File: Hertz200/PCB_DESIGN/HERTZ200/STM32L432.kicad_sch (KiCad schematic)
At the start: 16 parts, among them J6 Conn_01x07_Male, J7 Conn_01x03_Male, SW1 SW_Push, U1 STM32L431CCUx, U6 HTS221

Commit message: layout
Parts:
- FB1: footprint (none) -> Inductor_SMD:L_0603_1608Metric
- J6: value Conn_01x07_Male -> GPIO_PINS
- J7: value Conn_01x03_Male -> SWD_PINS
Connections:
- net GND: now also J6.1 (Pin_1)
- net SIM7020E_GPIO1: now also U1.32 (PA11); no longer U1.14 (PA4)
- net VIN: now reaches J6.2 (Pin_2)
- net GPIO01: now reaches J6.3 (Pin_3)
- net GPIO01: now also U1.14 (PA4)
- net PWR_SIGNAL: now reaches U1.45 (PB8)
- net PH3/BOOT0: no longer names the net of U1.44 (PH3)
- no-connect marks 17 -> 13
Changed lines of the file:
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@@
   )
   (no_connect (at 219.71 116.84))
+  (no_connect (at 119.38 71.12))
   (no_connect (at 129.54 55.88))
   (no_connect (at 119.38 116.84))
-  (no_connect (at 124.46 173.99))
-  (no_connect (at 124.46 171.45))
-  (no_connect (at 124.46 168.91))
   (no_connect (at 119.38 66.04))
   (no_connect (at 119.38 68.58))
@@
   (no_connect (at 149.86 86.36))
   (no_connect (at 149.86 88.9))
-  (no_connect (at 149.86 114.3))
   (no_connect (at 149.86 124.46))
-  (no_connect (at 119.38 106.68))
   (no_connect (at 119.38 109.22))
   (wire (pts (xy 204.47 55.88) (xy 215.9 55.88))
@@
     (stroke (width 0) (type default) (color 0 0 0 0))
   )
+  (wire (pts (xy 130.81 173.99) (xy 124.46 173.99))
+    (stroke (width 0) (type default) (color 0 0 0 0))
+  )
   (wire (pts (xy 176.53 63.5) (xy 179.07 63.5))
     (stroke (width 0) (type default) (color 0 0 0 0))
@@
     (stroke (width 1) (type default) (color 0 0 0 0))
   )
+  (wire (pts (xy 124.46 168.91) (xy 127 168.91))
+    (stroke (width 0) (type default) (color 0 0 0 0))
+  )
   (wire (pts (xy 134.62 52.07) (xy 134.62 54.61))
     (stroke (width 0) (type default) (color 0 0 0 0))
@@
     (stroke (width 0) (type default) (color 0 0 0 0))
   )
-  (wire (pts (xy 168.91 99.06) (xy 149.86 99.06))
-    (stroke (width 0) (type default) (color 0 0 0 0))
-  )
   (wire (pts (xy 250.19 116.84) (xy 252.73 116.84))
     (stroke (width 0) (type default) (color 0 0 0 0))
@@
     (stroke (width 0) (type default) (color 0 0 0 0))
   )
+  (wire (pts (xy 179.07 96.52) (xy 149.86 96.52))
+    (stroke (width 0) (type default) (color 0 0 0 0))
+  )
   (wire (pts (xy 215.9 55.88) (xy 215.9 58.42))
     (stroke (width 0) (type default) (color 0 0 0 0))
@@
     (effects (font (size 1.27 1.27)) (justify right bottom))
   )
+  (label "SWO" (at 102.87 93.98 180)
+    (effects (font (size 1.27 1.27)) (justify right bottom))
+  )
+  (label "GPIO04" (at 124.46 181.61 0)
+    (effects (font (size 1.27 1.27)) (justify left bottom))
+  )
+  (label "HTS221_SDA" (at 219.71 124.46 180)
+    (effects (font (size 1.27 1.27)) (justify right bottom))
+  )
+  (label "MCU_LED" (at 149.86 104.14 0)
+    (effects (font (size 1.27 1.27)) (justify left bottom))
+  )
+  (label "GPIO05" (at 124.46 184.15 0)
+    (effects (font (size 1.27 1.27)) (justify left bottom))
+  )
+  (label "GPIO03" (at 149.86 101.6 0)
+    (effects (font (size 1.27 1.27)) (justify left bottom))
+  )
+  (label "SWDIO" (at 166.37 119.38 0)
+    (effects (font (size 1.27 1.27)) (justify left bottom))
+  )
+  (label "SWCLK" (at 157.48 171.45 0)
+    (effects (font (size 1.27 1.27)) (justify left bottom))
+  )
+  (label "GPIO03" (at 124.46 179.07 0)
+    (effects (font (size 1.27 1.27)) (justify left bottom))
+  )
+  (label "VDD" (at 200.66 55.88 180)
+    (effects (font (size 1.27 1.27)) (justify right bottom))
+  )
+  (label "SWDIO" (at 157.48 173.99 0)
+    (effects (font (size 1.27 1.27)) (justify left bottom))
+  )
+  (label "VDD" (at 134.62 52.07 90)
+    (effects (font (size 1.27 1.27)) (justify left bottom))
+  )
+  (label "GPIO01" (at 130.81 173.99 0)
+    (effects (font (size 1.27 1.27)) (justify left bottom))
+  )
+  (label "NRST" (at 99.06 63.5 0)
+    (effects (font (size 1.27 1.27)) (justify left bottom))
+  )
+  (label "NRST" (at 119.38 60.96 180)
+    (effects (font (size 1.27 1.27)) (justify right bottom))
+  )
+  (label "SWCLK" (at 149.86 121.92 0)
+    (effects (font (size 1.27 1.27)) (justify left bottom))
+  )
+  (label "DRDY" (at 250.19 121.92 0)
+    (effects (font (size 1.27 1.27)) (justify left bottom))
+  )
   (label "GPIO02" (at 124.46 176.53 0)
     (effects (font (size 1.27 1.27)) (justify left bottom))
   )
-  (label "SWO" (at 102.87 93.98 180)
-    (effects (font (size 1.27 1.27)) (justify right bottom))
-  )
-  (label "GPIO04" (at 124.46 181.61 0)
-    (effects (font (size 1.27 1.27)) (justify left bottom))
-  )
-  (label "HTS221_SDA" (at 219.71 124.46 180)
-    (effects (font (size 1.27 1.27)) (justify right bottom))
-  )
-  (label "MCU_LED" (at 149.86 104.14 0)
-    (effects (font (size 1.27 1.27)) (justify left bottom))
-  )
-  (label "GPIO05" (at 124.46 184.15 0)
-    (effects (font (size 1.27 1.27)) (justify left bottom))
-  )
-  (label "GPIO03" (at 149.86 101.6 0)
-    (effects (font (size 1.27 1.27)) (justify left bottom))
-  )
-  (label "SWDIO" (at 166.37 119.38 0)
-    (effects (font (size 1.27 1.27)) (justify left bottom))
-  )
-  (label "SWCLK" (at 157.48 171.45 0)
-    (effects (font (size 1.27 1.27)) (justify left bottom))
-  )
-  (label "GPIO03" (at 124.46 179.07 0)
-    (effects (font (size 1.27 1.27)) (justify left bottom))
-  )
-  (label "PH3{slash}BOOT0" (at 119.38 71.12 180)
-    (effects (font (size 1.27 1.27)) (justify right bottom))
-  )
-  (label "VDD" (at 200.66 55.88 180)
-    (effects (font (size 1.27 1.27)) (justify right bottom))
-  )
-  (label "SWDIO" (at 157.48 173.99 0)
-    (effects (font (size 1.27 1.27)) (justify left bottom))
-  )
-  (label "GPIO02" (at 168.91 99.06 0)
-    (effects (font (size 1.27 1.27)) (justify left bottom))
-  )
-  (label "VDD" (at 134.62 52.07 90)
-    (effects (font (size 1.27 1.27)) (justify left bottom))
-  )
-  (label "NRST" (at 99.06 63.5 0)
-    (effects (font (size 1.27 1.27)) (justify left bottom))
-  )
-  (label "NRST" (at 119.38 60.96 180)
-    (effects (font (size 1.27 1.27)) (justify right bottom))
-  )
-  (label "SWCLK" (at 149.86 121.92 0)
-    (effects (font (size 1.27 1.27)) (justify left bottom))
-  )
-  (label "DRDY" (at 250.19 121.92 0)
-    (effects (font (size 1.27 1.27)) (justify left bottom))
-  )
   (label "VDDA" (at 176.53 63.5 180)
     (effects (font (size 1.27 1.27)) (justify right bottom))
   )
+  (label "GPIO01" (at 179.07 96.52 0)
+    (effects (font (size 1.27 1.27)) (justify left bottom))
+  )
   (label "HTS221_SCL" (at 119.38 119.38 180)
     (effects (font (size 1.27 1.27)) (justify right bottom))
@@
     (effects (font (size 1.27 1.27)) (justify right bottom))
   )
-  (global_label "SIM7020E_GPIO1" (shape bidirectional) (at 149.86 96.52 0) (fields_autoplaced)
-    (effects (font (size 1.27 1.27)) (justify left))
-    (property "Intersheet References" "${INTERSHEET_REFS}" (id 0) (at 168.1783 96.4406 0)
+  (label "GPIO02" (at 149.86 99.06 0)
+    (effects (font (size 1.27 1.27)) (justify left bottom))
+  )
+  (global_label "SIM7020E_GPIO1" (shape bidirectional) (at 149.86 114.3 0) (fields_autoplaced)
+    (effects (font (size 1.27 1.27)) (justify left))
+    (property "Intersheet References" "${INTERSHEET_REFS}" (id 0) (at 168.1783 114.2206 0)
+      (effects (font (size 1.27 1.27)) (justify left) hide)
+    )
+  )
+  (global_label "VIN" (shape input) (at 124.46 171.45 0) (fields_autoplaced)
+    (effects (font (size 1.27 1.27)) (justify left))
+    (property "Intersheet References" "${INTERSHEET_REFS}" (id 0) (at 129.8969 171.3706 0)
       (effects (font (size 1.27 1.27)) (justify left) hide)
     )
@@
     (property "Intersheet References" "${INTERSHEET_REFS}" (id 0) (at 166.485 116.7606 0)
       (effects (font (size 1.27 1.27)) (justify left) hide)
+    )
+  )
+  (global_label "PWR_SIGNAL" (shape input) (at 119.38 106.68 180) (fields_autoplaced)
+    (effects (font (size 1.27 1.27)) (justify right))
+    (property "Intersheet References" "${INTERSHEET_REFS}" (id 0) (at 105.4764 106.7594 0)
+      (effects (font (size 1.27 1.27)) (justify right) hide)
     )
   )
@@
     (in_bom yes) (on_board yes) (fields_autoplaced)
     (property "Reference" "J7" (id 0) (at 153.035 166.37 0))
-    (property "Value" "Conn_01x03_Male" (id 1) (at 153.035 168.91 0))
+    (property "Value" "SWD_PINS" (id 1) (at 153.035 168.91 0))
     (property "Footprint" "Connector_PinHeader_2.54mm:PinHeader_1x03_P2.54mm_Vertical" (id 2) (at 152.4 173.99 0)
       (effects (font (size 1.27 1.27)) hide)
@@
     (pin "2")
   )
+  (symbol (lib_id "power:GND") (at 127 168.91 90) (unit 1)
+    (in_bom yes) (on_board yes) (fields_autoplaced)
+    (property "Reference" "#PWR0104" (id 0) (at 133.35 168.91 0)
+      (effects (font (size 1.27 1.27)) hide)
+    )
+    (property "Value" "GND" (id 1) (at 130.81 168.9099 90)
+      (effects (font (size 1.27 1.27)) (justify right))
+    )
+    (property "Footprint" "" (id 2) (at 127 168.91 0)
+      (effects (font (size 1.27 1.27)) hide)
+    )
+    (property "Datasheet" "" (id 3) (at 127 168.91 0)
+      (effects (font (size 1.27 1.27)) hide)
+    )
+    (pin "1")
+  )
   (symbol (lib_id "Switch:SW_Push") (at 87.63 63.5 0) (unit 1)
     (in_bom yes) (on_board yes) (fields_autoplaced)
@@
       (effects (font (size 1.27 1.27)) (justify left))
     )
-    (property "Footprint" "" (id 2) (at 177.292 58.42 90)
+    (property "Footprint" "Inductor_SMD:L_0603_1608Metric" (id 2) (at 177.292 58.42 90)
       (effects (font (size 1.27 1.27)) hide)
     )
@@
     (in_bom yes) (on_board yes) (fields_autoplaced)
     (property "Reference" "J6" (id 0) (at 120.015 163.83 0))
-    (property "Value" "Conn_01x07_Male" (id 1) (at 120.015 166.37 0))
+    (property "Value" "GPIO_PINS" (id 1) (at 120.015 166.37 0))
     (property "Footprint" "Connector_PinHeader_2.54mm:PinHeader_1x07_P2.54mm_Vertical" (id 2) (at 119.38 176.53 0)
       (effects (font (size 1.27 1.27)) hide)

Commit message: layout02
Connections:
- net SWCLK: now also J7.2 (Pin_2); no longer J7.1 (Pin_1)
- net SWDIO: now also J7.1 (Pin_1); no longer J7.2 (Pin_2)
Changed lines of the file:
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@@
     (effects (font (size 1.27 1.27)) (justify left bottom))
   )
-  (label "SWCLK" (at 157.48 171.45 0)
+  (label "SWCLK" (at 157.48 173.99 0)
     (effects (font (size 1.27 1.27)) (justify left bottom))
   )
@@
     (effects (font (size 1.27 1.27)) (justify right bottom))
   )
-  (label "SWDIO" (at 157.48 173.99 0)
+  (label "SWDIO" (at 157.48 171.45 0)
     (effects (font (size 1.27 1.27)) (justify left bottom))
   )

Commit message: DRC
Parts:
- removed FB1: FerriteBead_Small, Inductor_SMD:L_0603_1608Metric, symbol Device:FerriteBead_Small
- removed SW1: SW_Push, TS04-66-75-BK-160-SMT:SW_TS04-66-75-BK-160-SMT, symbol Switch:SW_Push
- added R1: 0R, Resistor_SMD:R_0603_1608Metric, symbol Device:R_Small
- added S1: TL3305AF160QG, TL3305AF160QG:SW_TL3305AF160QG, symbol TL3305AF160QG:TL3305AF160QG
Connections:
- net GPIO04 is gone; now on net GPIO05: J6.6 (Pin_6)
- net GPIO4 is gone; now on net GPIO05: U1.18 (PB0)
- net VIN is gone; now on net +3V3: J6.2 (Pin_2)
- net +3V3: now also R1.1
- net DRDY: now also U1.25 (PB12)
- net GND: now also J6.7 (Pin_7), S1.3, S1.4
- net GPIO05: no longer J6.7 (Pin_7)
- net NRST: now also S1.1, S1.2
- net VDDA: now also R1.2
- net GPIO5: no longer names the net of U1.19 (PB1)
- net PWR_SIGNAL renamed Signal_VOUT
- no-connect marks 13 -> 12

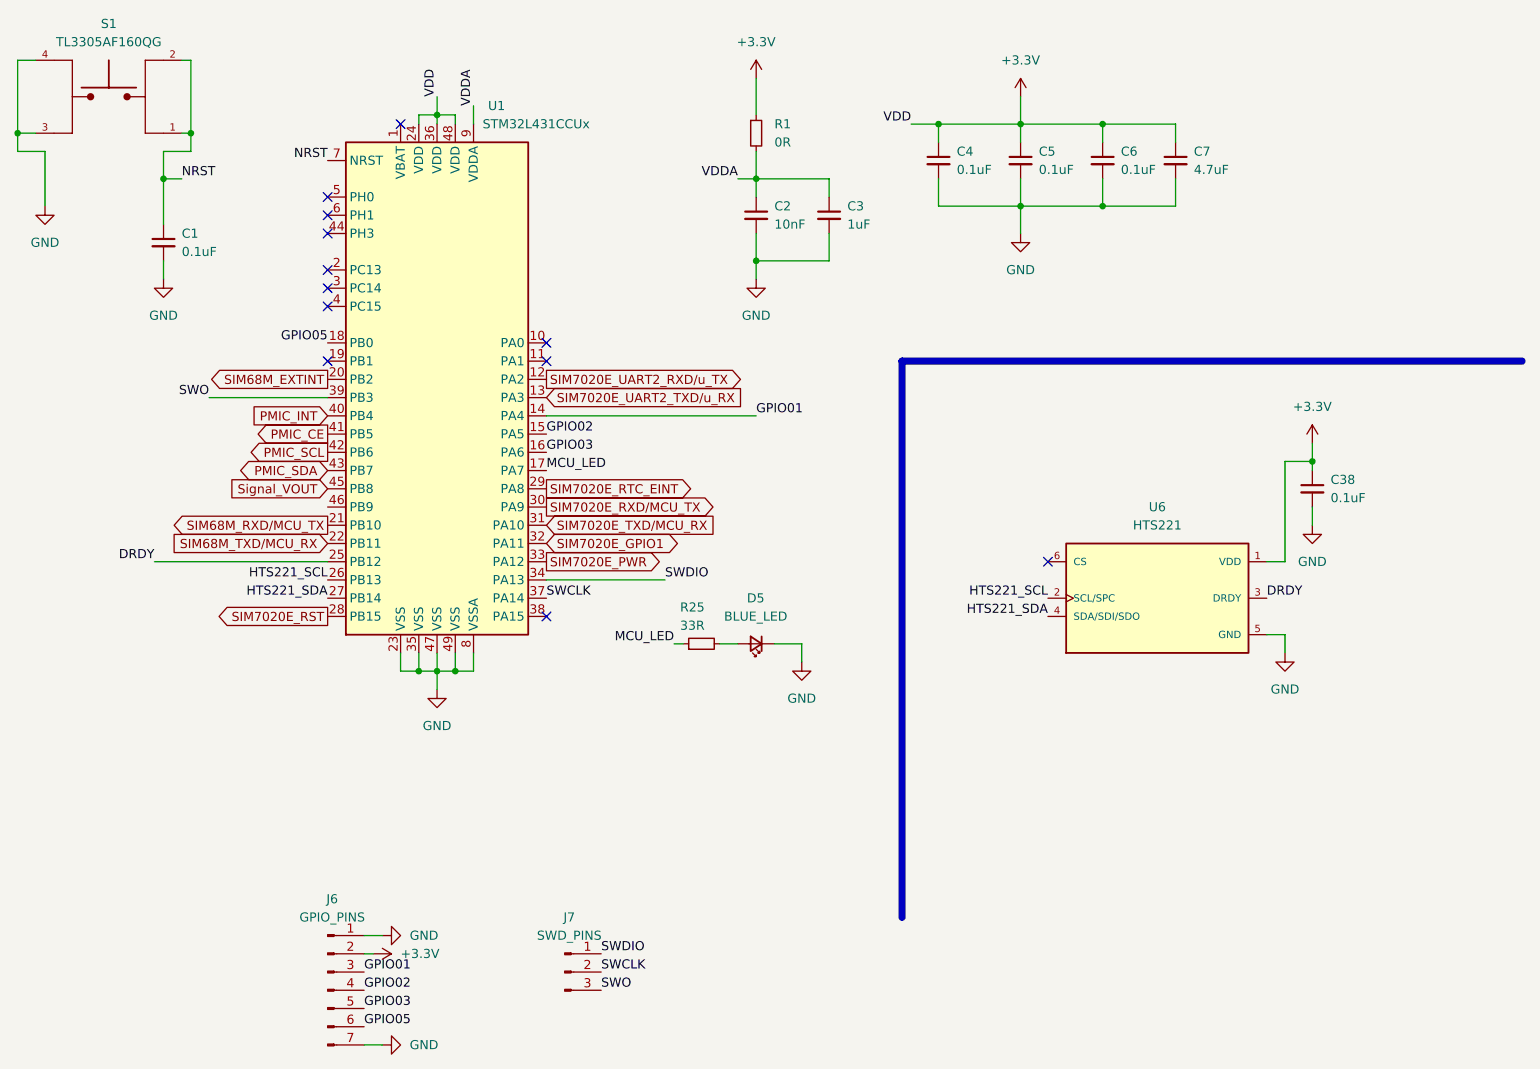
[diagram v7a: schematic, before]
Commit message: TEMPERATURE SENSOR ROUTING
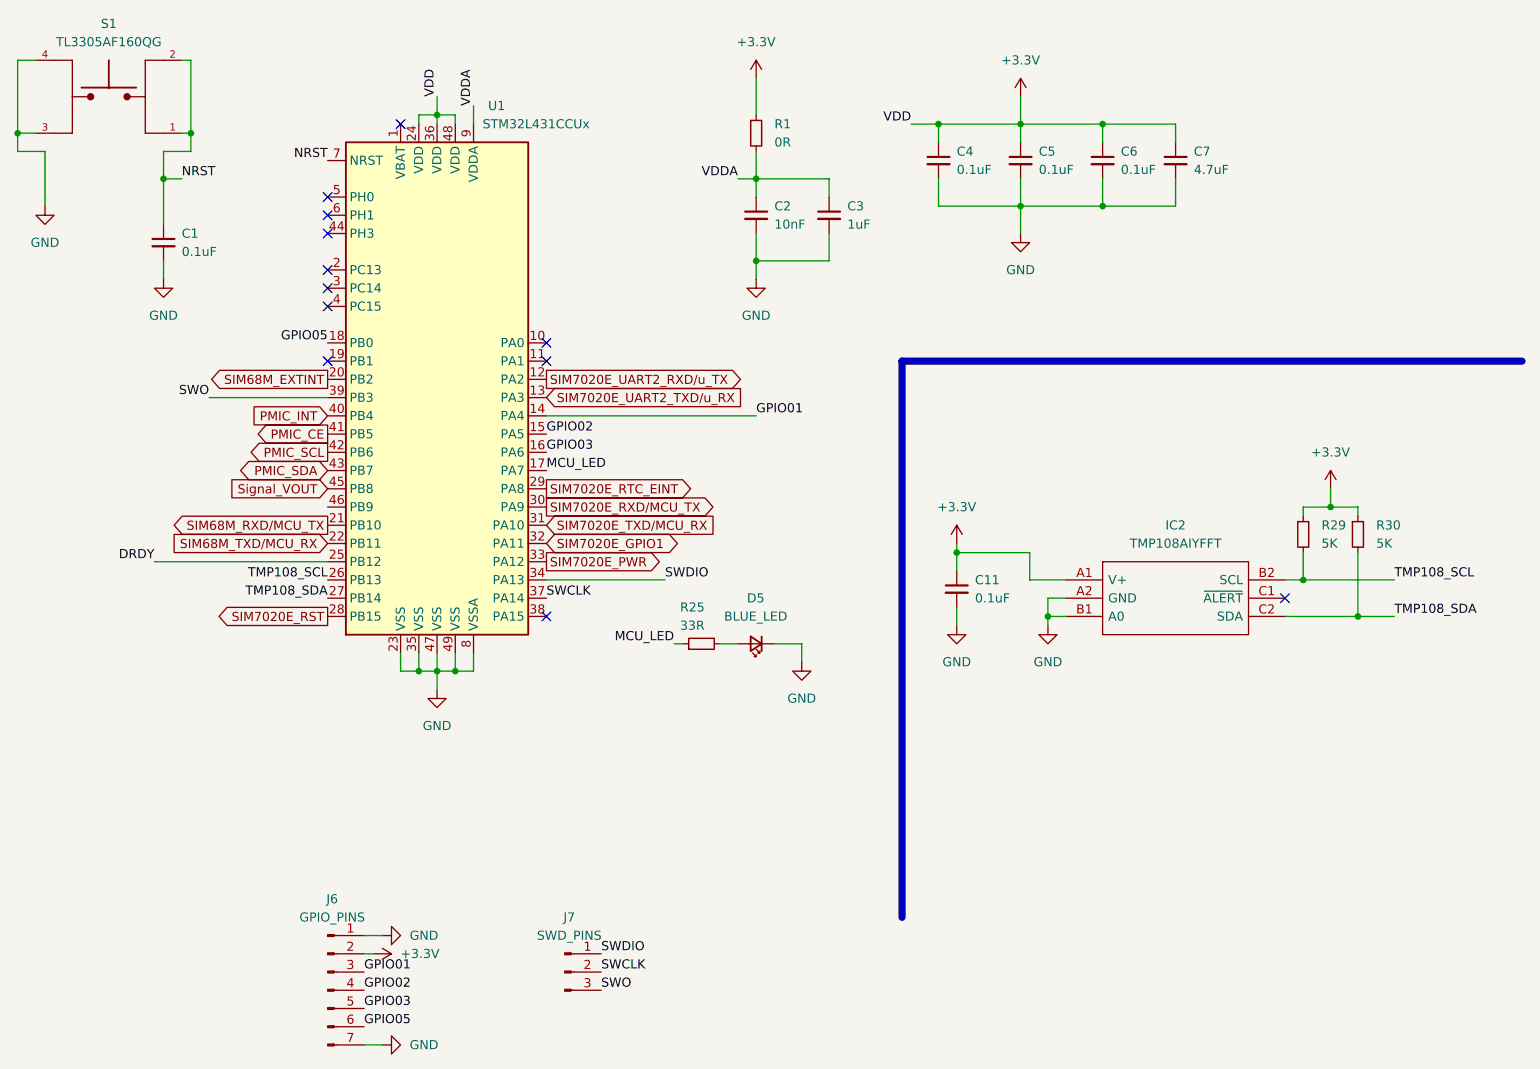
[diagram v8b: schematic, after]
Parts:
- removed C38: 0.1uF, Capacitor_SMD:C_0603_1608Metric, symbol Device:C_Small
- removed U6: HTS221, HTS221:XDCR_HTS221, symbol HTS221:HTS221
- added C11: 0.1uF, Capacitor_SMD:C_0603_1608Metric, symbol Device:C_Small
- added IC2: TMP108AIYFFT, TMP108:TMP108AIYFFT, symbol TMP108AIYFFT:TMP108AIYFFT
- added R29, R30: 5K, Resistor_SMD:R_0603_1608Metric, symbol Device:R_Small
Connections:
- net +3V3: now also C11.1, IC2.A1 (V+), R29.1, R30.1
- net GND: now also C11.2, IC2.A2 (GND), IC2.B1 (A0)
- net HTS221_SCL renamed TMP108_SCL
- net TMP108_SCL: now also IC2.B2 (SCL), R29.2
- net HTS221_SDA renamed TMP108_SDA
- net TMP108_SDA: now also IC2.C2 (SDA), R30.2
